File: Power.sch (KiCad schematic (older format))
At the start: 13 parts, among them J14 Conn_01x02, Q5 AO3401A, U4 TPS62130

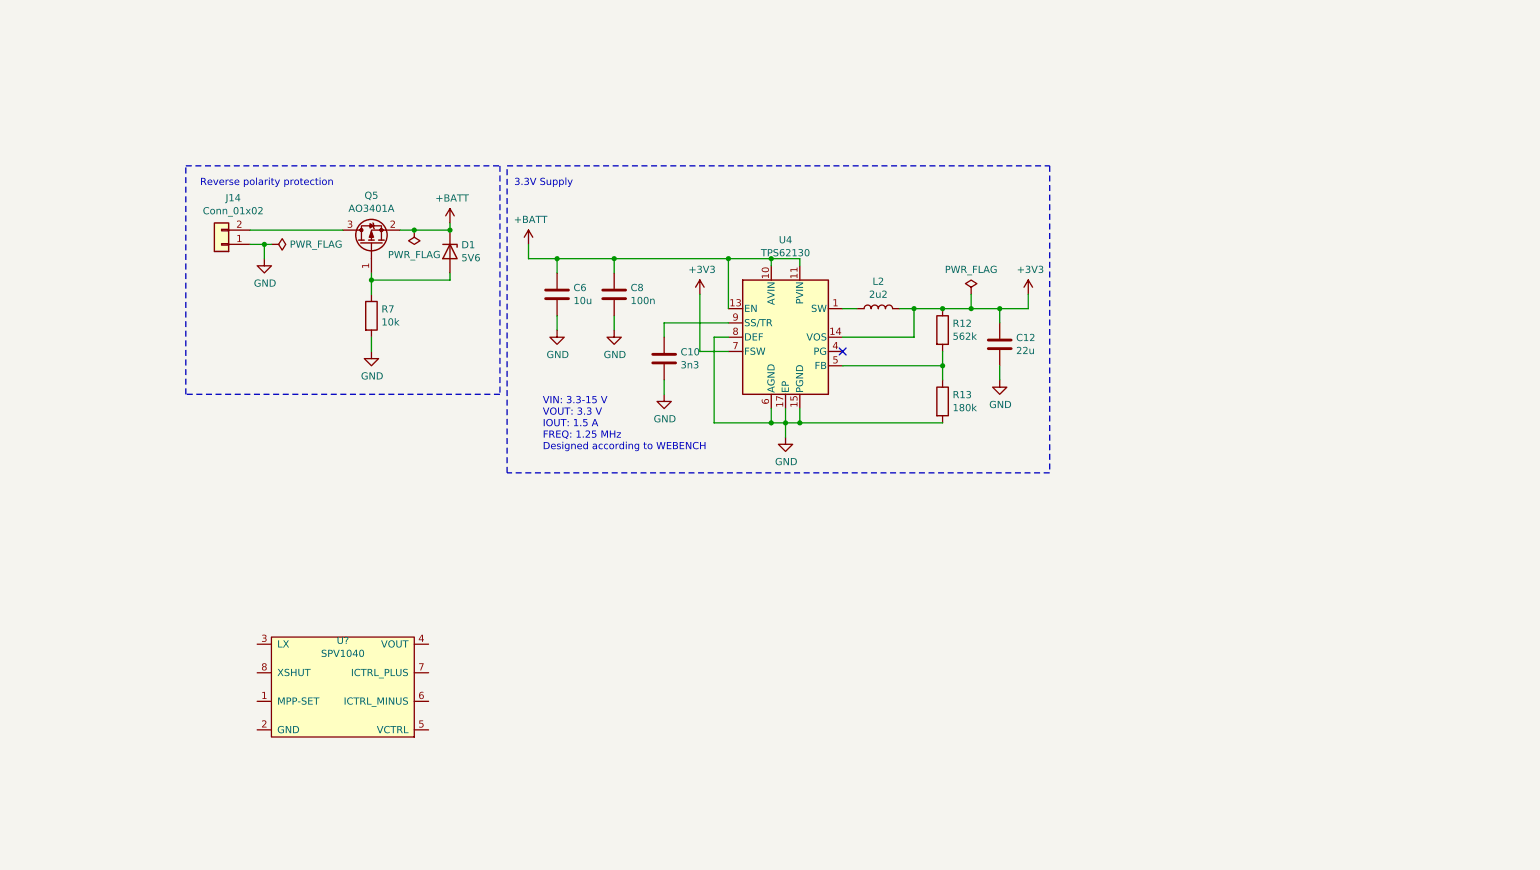
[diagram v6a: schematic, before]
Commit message: Add MPPT battery charger and polyfuse, replace reverse polarity
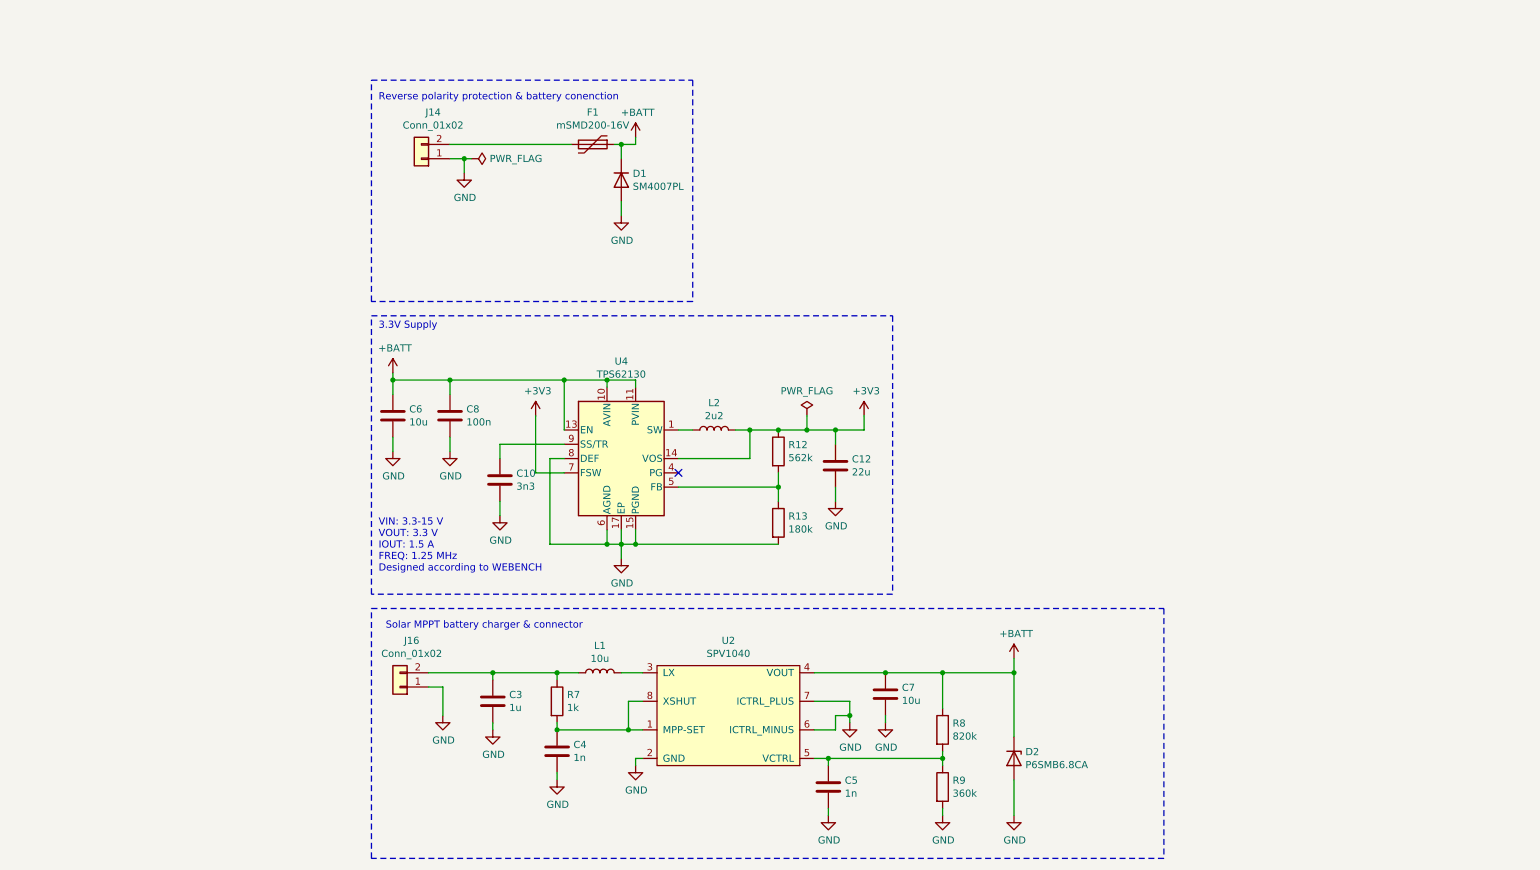
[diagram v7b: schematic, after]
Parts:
- removed D1: 5V6, Diode_SMD:D_MiniMELF, symbol Device:D_Zener
- removed Q5: AO3401A, Package_TO_SOT_SMD:SOT-23, symbol Transistor_FET:AO3401A
- removed U?: SPV1040, Package_SO:TSSOP-8_4.4x3mm_P0.65mm, symbol co2_sensor_node:SPV1040
- added C3: 1u, Capacitor_SMD:C_0603_1608Metric, symbol Device:C
- added C4, C5: 1n, Capacitor_SMD:C_0603_1608Metric, symbol Device:C
- added C7: 10u, Capacitor_SMD:C_0805_2012Metric, symbol Device:C
- added D1: SM4007PL, Diode_SMD:D_SOD-123F, symbol Device:D
- added D2: P6SMB6.8CA, Diode_SMD:D_SMB, symbol Device:D_Zener
- added F1: mSMD200-16V, Fuse:Fuse_1812_4532Metric, symbol Device:Polyfuse
- added J16: Conn_01x02, Connector_JST:JST_XH_B2B-XH-AM_1x02_P2.50mm_Vertical, symbol Connector_Generic:Conn_01x02
- added L1: 10u, symbol Device:L
- added R8: 820k, Resistor_SMD:R_0603_1608Metric, symbol Device:R
- added R9: 360k, Resistor_SMD:R_0603_1608Metric, symbol Device:R
- added U2: SPV1040, Package_SO:TSSOP-8_4.4x3mm_P0.65mm, symbol co2_sensor_node:SPV1040
- R7: value 10k -> 1k; LCSC C25804 -> C21190
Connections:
- net +BATT: now also C7.1, D1.1 (K), D2.1 (K), F1.1, R8.1, U2.4 (VOUT)
- net GND: now also C3.2, C4.2, C5.2, C7.2, D1.2 (A), D2.2 (A), J16.1 (Pin_1), R9.2, U2.2 (GND), U2.6 (ICTRL_MINUS), U2.7 (ICTRL_PLUS); no longer R7.2
- net at R7.1: now also C3.1, J16.2 (Pin_2), L1.1
- net at J14.2 (Pin_2): now also F1.2
- new net: C4.1, R7.2, U2.1 (MPP-SET), U2.8 (XSHUT)
- new net: L1.2, U2.3 (LX)
- new net: C5.1, R8.2, R9.1, U2.5 (VCTRL)
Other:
- note added: "Reverse polarity protection & battery conenction"
- note added: "Solar MPPT battery charger & connector"
- note removed: "Reverse polarity protection"
- moved on the sheet: C10, C12, C6, C8, J14, L2, R12, R13, U4
